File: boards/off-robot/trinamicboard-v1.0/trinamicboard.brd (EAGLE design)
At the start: 121.9 x 77.4 mm, 54 parts, among them J4 DF22-2, J5 4-PIN_2MM-H, J6 MKS-1658, U1 ADC124S101, U2 SN74LVC3G17, U3 SN74LVC3G17, U4 VND5E006ASPTR-E, U5 MPM3620GQV-P, U6 MPM3620GQV-P

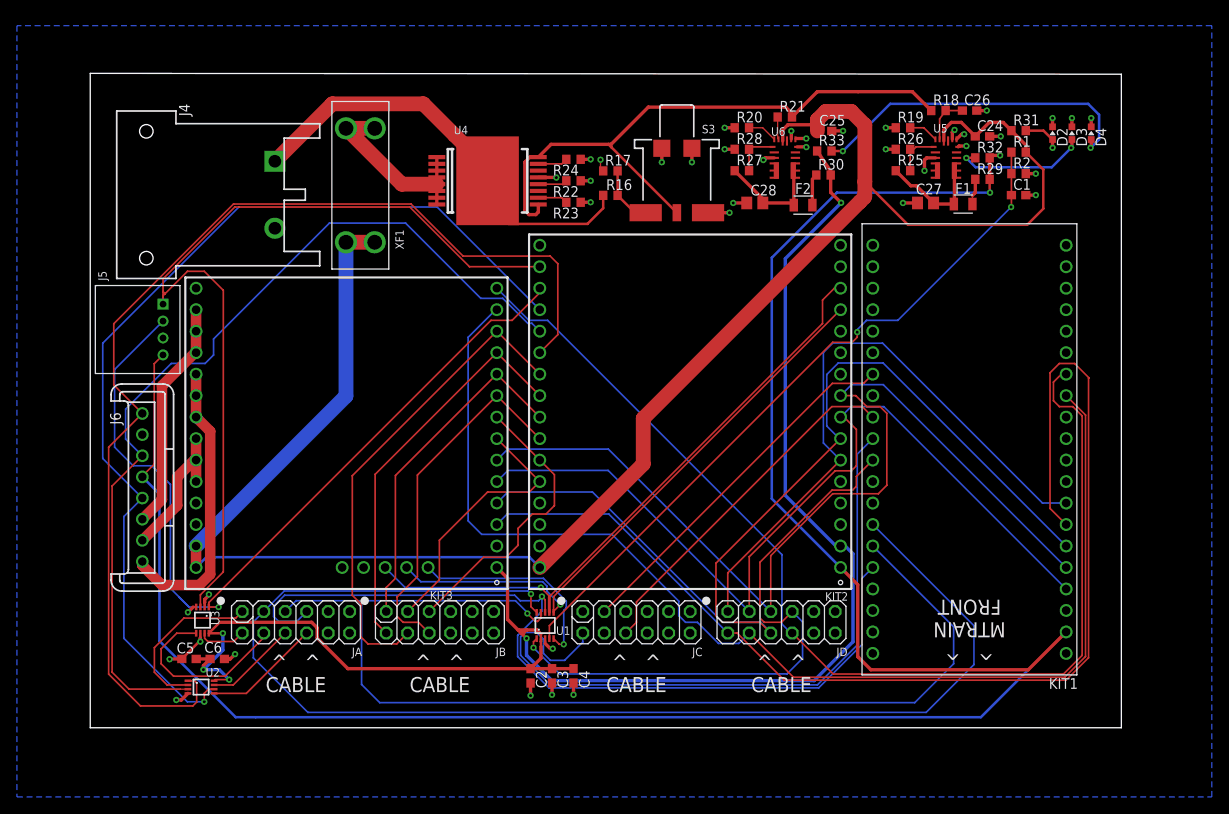
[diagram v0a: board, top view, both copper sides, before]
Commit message: Fixed ERC/DRC issues
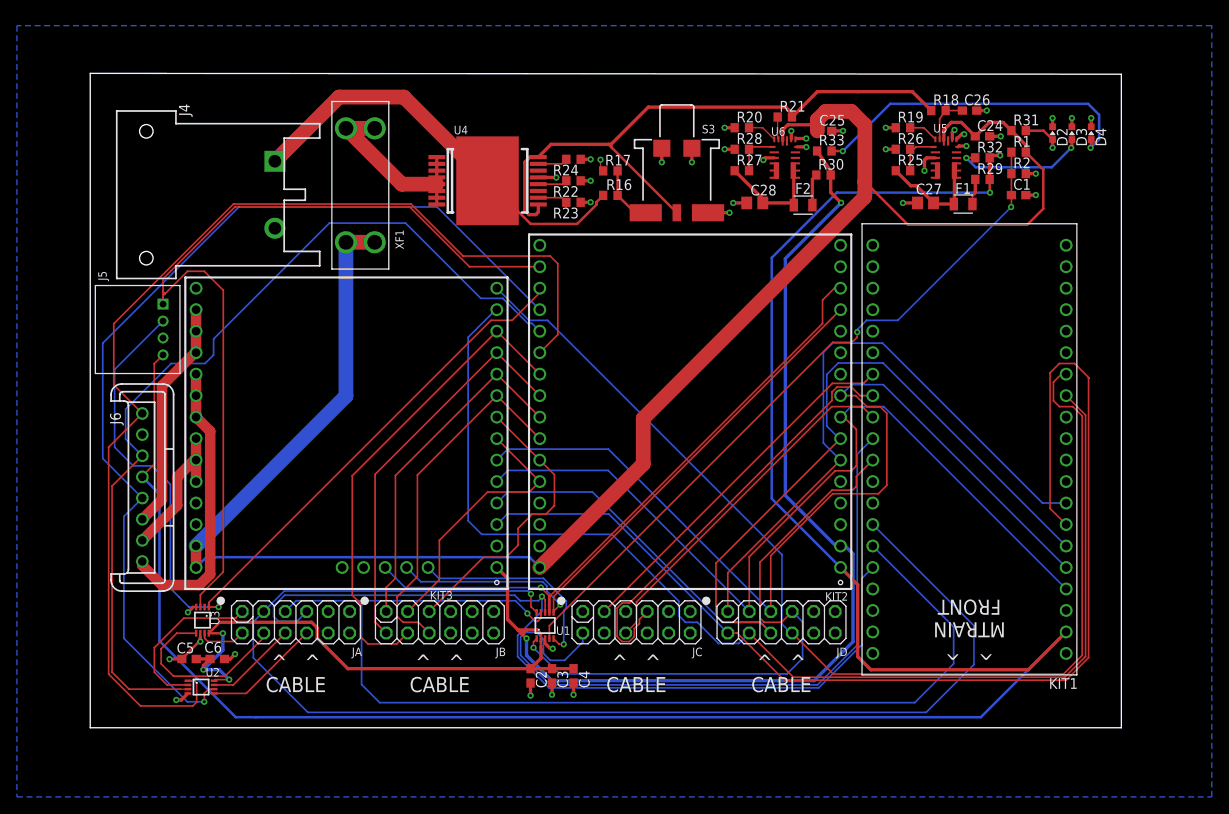
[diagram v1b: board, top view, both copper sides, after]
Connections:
- removed net MISO-FPA: KIT1.P$28
- net GND: no longer U3.2
- net MISO-FPGA: now also KIT1.P$28
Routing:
- net MISO-FPGA: track 0.00 -> 51.5 mm
- net VIN: track 79.9 -> 49.7 mm
- net GND: track 61.9 -> 59.9 mm, vias 40 -> 39
- net ENC-A: track 102.8 -> 101.1 mm
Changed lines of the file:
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@@
 <contactref element="U3" pad="4"/>
 <contactref element="U3" pad="6"/>
-<contactref element="U3" pad="2"/>
 <contactref element="C5" pad="2"/>
 <contactref element="C6" pad="2"/>
@@
 <wire x1="40.236" y1="46.401" x2="41.418" y2="46.401" width="0.4" layer="1"/>
 <via x="-53.032" y="-12.919" extent="1-16" drill="0.35"/>
-<via x="-50.554" y="-10.803" extent="1-16" drill="0.35"/>
 <via x="-51.562" y="-16.383" extent="1-16" drill="0.35"/>
-<wire x1="-51.054" y1="-12.289" x2="-51.058" y2="-12.293" width="0.1524" layer="1"/>
 <wire x1="-51.562" y1="-15.397" x2="-51.558" y2="-15.393" width="0.1524" layer="1"/>
 <via x="-54.405" y="-23.282" extent="1-16" drill="0.35"/>
@@
 <wire x1="-51.562" y1="-16" x2="-51.562" y2="-15.94536875" width="0.4" layer="1"/>
 <wire x1="-51.562" y1="-15.94536875" x2="-51.558" y2="-15.94136875" width="0.4" layer="1"/>
-<wire x1="-50.554" y1="-10.803" x2="-50.554" y2="-10.903" width="0.4" layer="1"/>
-<wire x1="-50.554" y1="-10.903" x2="-51.054" y2="-11.403" width="0.4" layer="1"/>
-<wire x1="-51.054" y1="-11.403" x2="-51.054" y2="-11.74063125" width="0.4" layer="1"/>
-<wire x1="-51.054" y1="-11.74063125" x2="-51.058" y2="-11.74463125" width="0.4" layer="1"/>
 <wire x1="-53.032" y1="-12.919" x2="-52.406" y2="-12.293" width="0.4" layer="1"/>
 <wire x1="-10.799" y1="-16.314" x2="-10.799" y2="-16.028" width="0.2" layer="1"/>
-<wire x1="-51.058" y1="-12.293" x2="-51.058" y2="-12" width="0.2" layer="1"/>
-<wire x1="-51.058" y1="-12" x2="-51.058" y2="-11.74463125" width="0.2" layer="1"/>
 <wire x1="-51.562" y1="-16" x2="-51.562" y2="-15.397" width="0.2" layer="1"/>
-<wire x1="-51.058" y1="-12" x2="-51.054" y2="-12.004" width="0.1524" layer="1"/>
-<wire x1="-51.054" y1="-12.004" x2="-51.054" y2="-12.289" width="0.1524" layer="1"/>
 <wire x1="-10.186" y1="-17.214" x2="-9.899" y2="-17.214" width="0.4" layer="1"/>
 <wire x1="-10.799" y1="-16.601" x2="-10.186" y2="-17.214" width="0.4" layer="1"/>
@@
 <wire x1="25.4" y1="46.3" x2="27" y2="44.7" width="1.75" layer="1"/>
 <wire x1="27" y1="36.2" x2="26.9" y2="36.1" width="0.3" layer="1"/>
-<wire x1="26.4" y1="35.6" x2="26.9" y2="36.1" width="1.75" layer="1"/>
-<wire x1="26.4" y1="35.6" x2="0.8" y2="10" width="1.75" layer="1"/>
+<wire x1="26.9" y1="36.1" x2="0.8" y2="10" width="1.75" layer="1"/>
 <wire x1="0.8" y1="10" x2="0.8" y2="4.61" width="1.75" layer="1"/>
 <wire x1="0.8" y1="4.61" x2="-11.43" y2="-7.62" width="1.75" layer="1"/>
@@
 <wire x1="21.391" y1="43.988" x2="21.391" y2="45.314" width="1.75" layer="1"/>
 <wire x1="21.391" y1="45.314" x2="22.377" y2="46.3" width="1.75" layer="1"/>
-<wire x1="26.4" y1="35.6" x2="26.7" y2="35.3" width="0.3" layer="1"/>
 <wire x1="-52.07" y1="-7.62" x2="-50.85" y2="-6.4" width="0.3" layer="16"/>
 <wire x1="-12.65" y1="-6.4" x2="-11.43" y2="-7.62" width="0.3" layer="16"/>
@@
 <contactref element="R16" pad="2"/>
 <contactref element="U4" pad="17"/>
-<wire x1="-15.7" y1="40.005" x2="-17.605" y2="38.1" width="1.75" layer="1"/>
-<wire x1="-42.75" y1="40.41" x2="-35.96" y2="47.2" width="1.75" layer="1"/>
-<wire x1="-35.96" y1="47.2" x2="-25.2" y2="47.2" width="1.75" layer="1"/>
-<wire x1="-25.2" y1="47.2" x2="-21.5" y2="43.5" width="1.75" layer="1"/>
-<wire x1="-21.5" y1="43.5" x2="-19" y2="41" width="1.75" layer="1"/>
-<wire x1="-17.605" y1="38.1" x2="-18" y2="37.705" width="1.75" layer="1"/>
-<wire x1="-18" y1="37.705" x2="-18" y2="34" width="1.75" layer="1"/>
-<wire x1="-18" y1="34" x2="-20" y2="34" width="1.75" layer="1"/>
-<wire x1="-20" y1="34" x2="-20" y2="35" width="1.75" layer="1"/>
-<wire x1="-20" y1="35" x2="-17" y2="38" width="1.75" layer="1"/>
-<wire x1="-17" y1="38" x2="-15" y2="38" width="1.75" layer="1"/>
-<wire x1="-15" y1="38" x2="-15" y2="37" width="1.75" layer="1"/>
-<wire x1="-15" y1="37" x2="-15.75" y2="37.75" width="1.75" layer="1"/>
-<wire x1="-15.75" y1="37.75" x2="-15.75" y2="41.75" width="1.75" layer="1"/>
-<wire x1="-17.605" y1="38.1" x2="-17.605" y2="39.4358" width="0.3" layer="1"/>
-<wire x1="-17.605" y1="38.1" x2="-17.605" y2="38.605" width="0.3" layer="1"/>
-<wire x1="-17.605" y1="38.605" x2="-18" y2="39" width="0.3" layer="1"/>
-<wire x1="-18" y1="39" x2="-18" y2="38.495" width="0.3" layer="1"/>
-<wire x1="-18" y1="38.495" x2="-17.605" y2="38.1" width="0.3" layer="1"/>
-<wire x1="-3.932" y1="36.374" x2="-3.932" y2="34.868" width="0.3" layer="1"/>
-<wire x1="-5.8" y1="33" x2="-15.1" y2="33" width="0.3" layer="1"/>
-<wire x1="-15.1" y1="33" x2="-17.605" y2="35.505" width="0.3" layer="1"/>
-<wire x1="-17.605" y1="35.505" x2="-17.605" y2="37" width="0.3" layer="1"/>
-<wire x1="-17.605" y1="37" x2="-17.605" y2="38.1" width="0.3" layer="1"/>
-<wire x1="-3.932" y1="34.868" x2="-5.8" y2="33" width="0.3" layer="1"/>
-<wire x1="-19" y1="41" x2="-17" y2="39" width="1.75" layer="1"/>
-<wire x1="-17" y1="39" x2="-17" y2="37" width="1.75" layer="1"/>
-<wire x1="-17" y1="37" x2="-17.605" y2="37" width="1.75" layer="1"/>
+<wire x1="-17.605" y1="38.1" x2="-27.505" y2="48" width="1.75" layer="1"/>
+<wire x1="-35.16" y1="48" x2="-42.75" y2="40.41" width="1.75" layer="1"/>
+<wire x1="-27.505" y1="48" x2="-35.16" y2="48" width="1.75" layer="1"/>
+<wire x1="-3.932" y1="36.374" x2="-4.7324" y2="35.5736" width="0.3" layer="1"/>
+<wire x1="-4.7324" y1="35.5736" x2="-4.7324" y2="35.27808125" width="0.3" layer="1"/>
+<wire x1="-4.7324" y1="35.27808125" x2="-7.01048125" y2="33" width="0.3" layer="1"/>
+<wire x1="-12.505" y1="33" x2="-17.605" y2="38.1" width="0.3" layer="1"/>
+<wire x1="-7.01048125" y1="33" x2="-12.505" y2="33" width="0.3" layer="1"/>
 </signal>
 <signal name="CS2">
@@
 <wire x1="-61.7" y1="15.786" x2="-61.7" y2="6.6" width="0.2" layer="16"/>
 <wire x1="-55.1" y1="-10.0884" x2="-54.0942" y2="-11.0942" width="0.2" layer="16"/>
-<wire x1="-54.0942" y1="-11.0942" x2="-52.9" y2="-12.2884" width="0.2" layer="16"/>
 <wire x1="-61.7" y1="6.6" x2="-59.5" y2="4.4" width="0.2" layer="16"/>
 <wire x1="-59.5" y1="4.4" x2="-57.3" y2="4.4" width="0.2" layer="16"/>
@@
 <wire x1="23.1" y1="11.4" x2="26.7" y2="11.4" width="0.2" layer="1"/>
 </signal>
-<signal name="MISO-FPA">
-<contactref element="KIT1" pad="P$28"/>
-</signal>
 <signal name="MOSI-FPGA">
 <contactref element="KIT1" pad="P$27"/>
@@
 <signal name="MISO-FPGA">
 <contactref element="JC" pad="4"/>
+<contactref element="KIT1" pad="P$28"/>
+<wire x1="27.94" y1="12.7" x2="26.42943125" y2="12.7" width="0.2" layer="1"/>
+<wire x1="23.70981875" y1="13.7144" x2="23.1156" y2="13.12018125" width="0.2" layer="1"/>
+<wire x1="23.1156" y1="13.12018125" x2="23.1156" y2="12.1156" width="0.2" layer="1"/>
+<wire x1="26.42943125" y1="12.7" x2="25.41503125" y2="13.7144" width="0.2" layer="1"/>
+<wire x1="25.41503125" y1="13.7144" x2="23.70981875" y2="13.7144" width="0.2" layer="1"/>
+<wire x1="-1.69018125" y1="-11.8126" x2="-2.2844" y2="-12.40681875" width="0.2" layer="1"/>
+<wire x1="-2.2844" y1="-15.78718125" x2="-1.69018125" y2="-16.3814" width="0.2" layer="1"/>
+<wire x1="-1.69018125" y1="-16.3814" x2="-0.84981875" y2="-16.3814" width="0.2" layer="1"/>
+<wire x1="-0.84981875" y1="-16.3814" x2="-0.2556" y2="-15.78718125" width="0.2" layer="1"/>
+<wire x1="-0.2556" y1="-14.850975" x2="0.3524" y2="-14.242975" width="0.2" layer="1"/>
+<wire x1="-0.2556" y1="-15.78718125" x2="-0.2556" y2="-14.850975" width="0.2" layer="1"/>
+<wire x1="-0.8126" y1="-11.8126" x2="-1.69018125" y2="-11.8126" width="0.2" layer="1"/>
+<wire x1="0.3524" y1="-14.242975" x2="0.3524" y2="-13.7446" width="0.2" layer="1"/>
+<wire x1="0.3524" y1="-13.7446" x2="1.27" y2="-12.827" width="0.2" layer="1"/>
+<wire x1="-2.2844" y1="-12.40681875" x2="-2.2844" y2="-15.78718125" width="0.2" layer="1"/>
+<wire x1="23.1156" y1="12.1156" x2="-0.8126" y2="-11.8126" width="0.2" layer="1"/>
 </signal>
 </signals>

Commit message: Fixed trace sizing, but have clearance issues
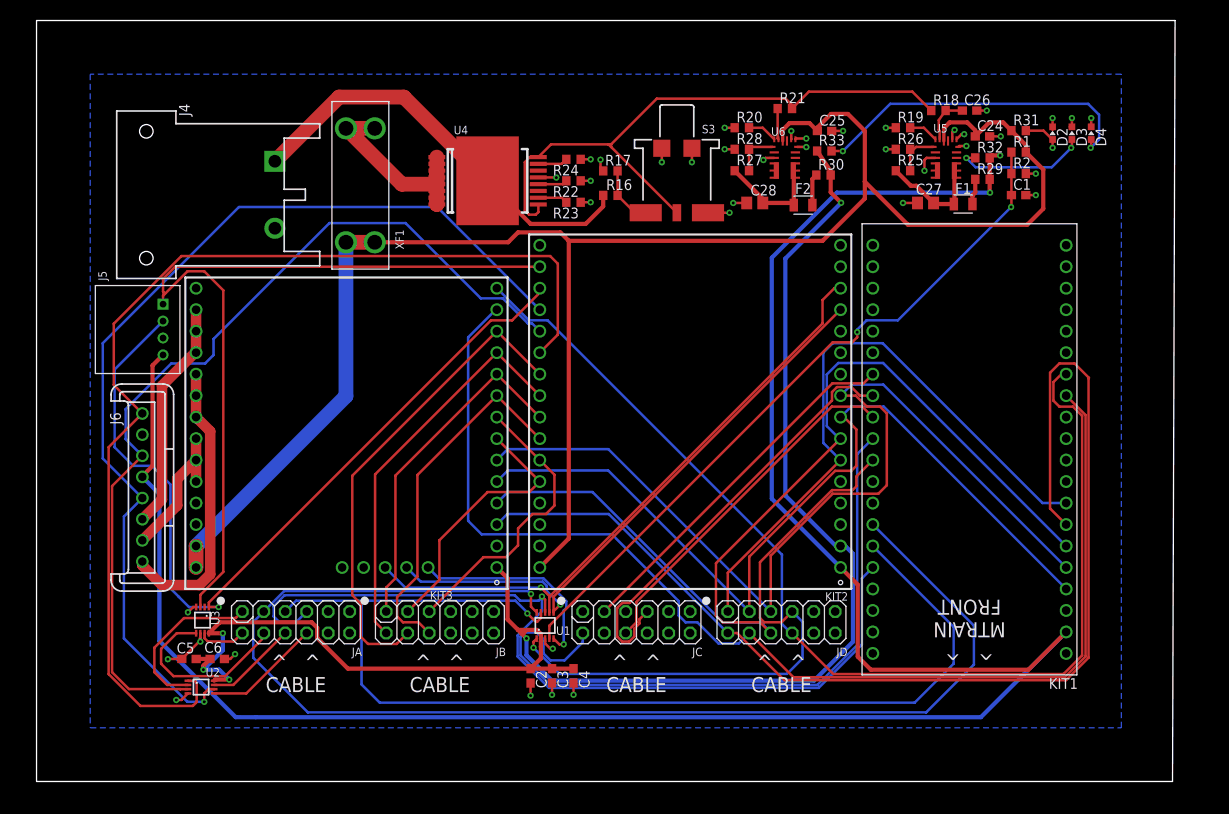
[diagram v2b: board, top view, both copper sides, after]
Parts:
- moved R21 1.00 mm to (17.5, 46.6)
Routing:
- net ENC-B: track 103.2 -> 97.3 mm
- net H1: track 132.7 -> 127.6 mm
- net VBATT: track 22.5 -> 25.7 mm
- net EN1: track 2.67 -> 3.67 mm
- net +18.5V: track 219.3 -> 218.5 mm
- net VIN: track 49.7 -> 50.3 mm
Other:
- board size 121.9 x 77.4 mm -> 134.6 x 90 mm

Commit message: Fixed 190 clearance issues
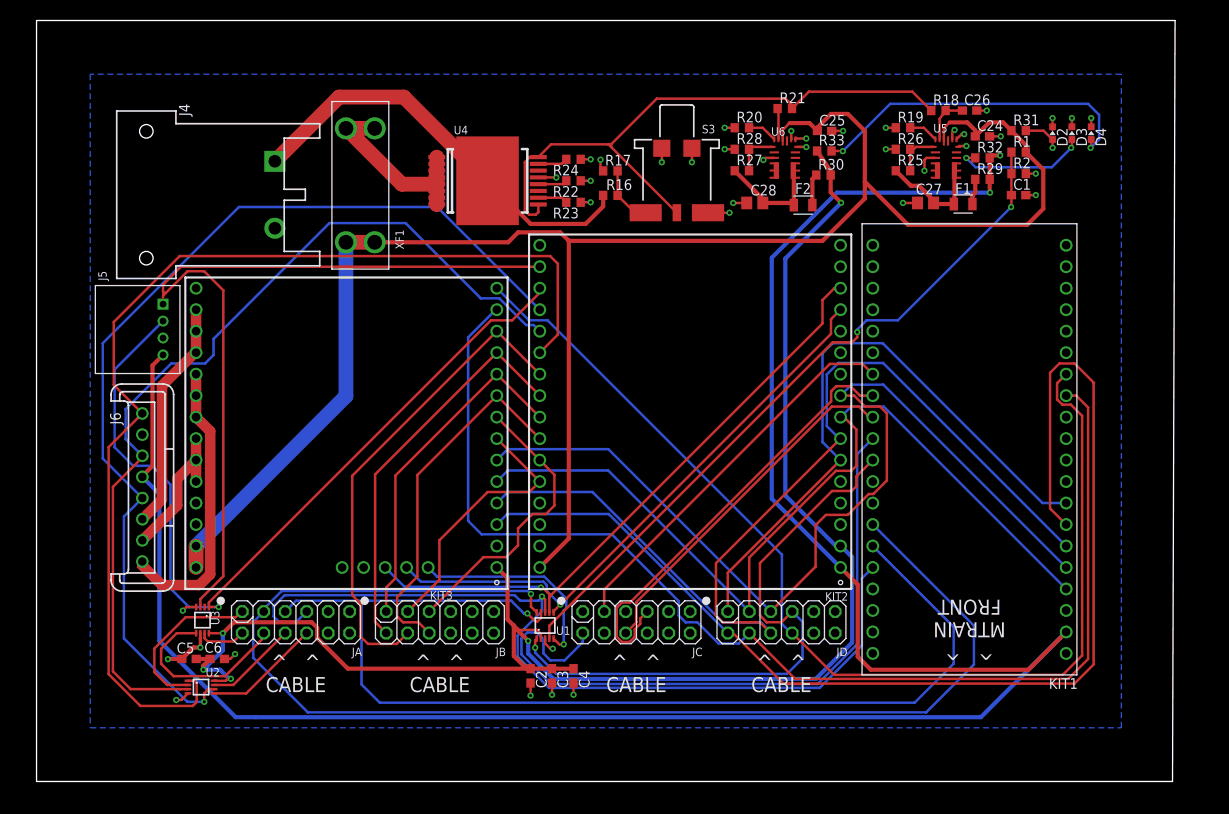
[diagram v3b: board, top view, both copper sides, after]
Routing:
- net MOSI-FPGA: track 43.4 -> 45.9 mm
- net !SS!-6200: track 137.3 -> 139.0 mm
- net DRV_EN: track 141.9 -> 143.4 mm
- net MISO-TMC: track 115.6 -> 114.3 mm
- net CURV: track 71.4 -> 70.2 mm
- net +3.3V: track 189.7 -> 188.7 mm
- net FAULT: track 130.4 -> 129.4 mm
- net GND: track 60.1 -> 61.0 mm
- net !SS!-FPGA: track 82.5 -> 81.9 mm

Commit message: Added mouting holes Added silkscreen details Modified TMCs footprint to add tPlace layer
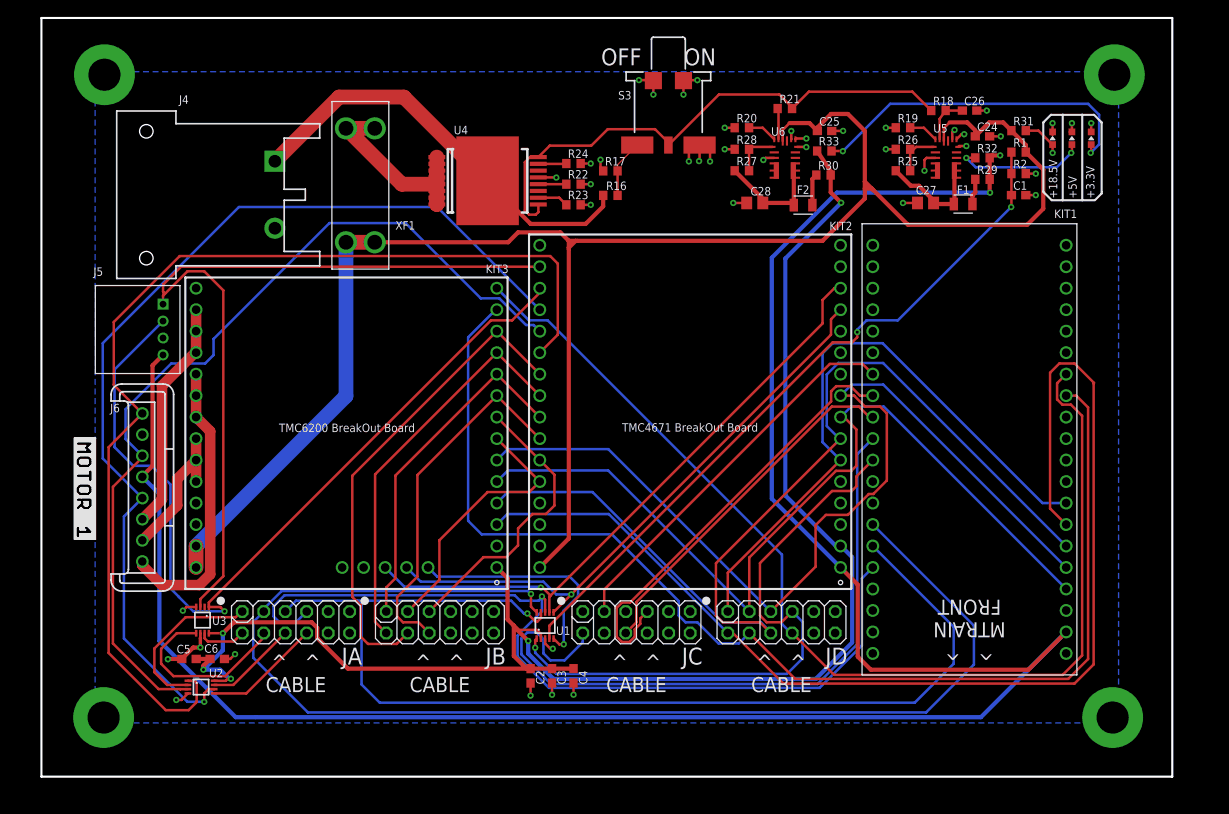
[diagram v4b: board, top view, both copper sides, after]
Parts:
- added U$11: (no value), RoboJackets-Aesthetics:ROBOBUZZ_1.0X2
- added U$2: (no value), RoboJackets-Aesthetics:ROBOJACKETS
- added U$3: (no value), RoboJackets-Aesthetics:MOTOR-1
- moved S3 8.06 mm to (3.78, 42.3)
- moved D2 0.60 mm to (49.2, 43.1)
- moved D3 0.60 mm to (51.5, 43.1)
- moved D4 0.60 mm to (53.8, 43.1)
- moved R24 0.50 mm to (-7.45, 40.1)
- moved R22 0.40 mm to (-7.45, 37.7)
- moved R23 0.30 mm to (-7.45, 35.3)
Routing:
- net EN-PWR: track 74.0 -> 64.1 mm
- net GND: track 61.0 -> 65.9 mm, vias 39 -> 43
- net CURW: track 24.9 -> 27.8 mm
- net H2: track 107.5 -> 105.6 mm
- net +18.5V: track 218.5 -> 220.5 mm
- net ENC-A: track 101.1 -> 103.0 mm
- net H1: track 127.7 -> 126.7 mm
- net +3.3V-LED: track 39.8 -> 40.4 mm
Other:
- board size 134.6 x 90 mm -> 133.7 x 89.7 mm
- board text added: "+18.5V"
- board text added: "+3.3V"
- board text added: "+5V"
- board text added: "OFF"
- board text added: "ON"
- board text added: "Trinamic"
- board text added: "v1.0"
